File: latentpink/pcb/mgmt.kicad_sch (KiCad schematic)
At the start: 56 parts, among them J10 XILINX_JTAG, J11 FAN_01, J12 FAN_01, J15 CONN_01X03, J16 JUMPER_0402_SPDT, J17 JUMPER_0402_SPDT, J7 RJ45, U2 XC7K160T-2FBG484C, U20 AT24MAC402, U23 ADM3101E_QFN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

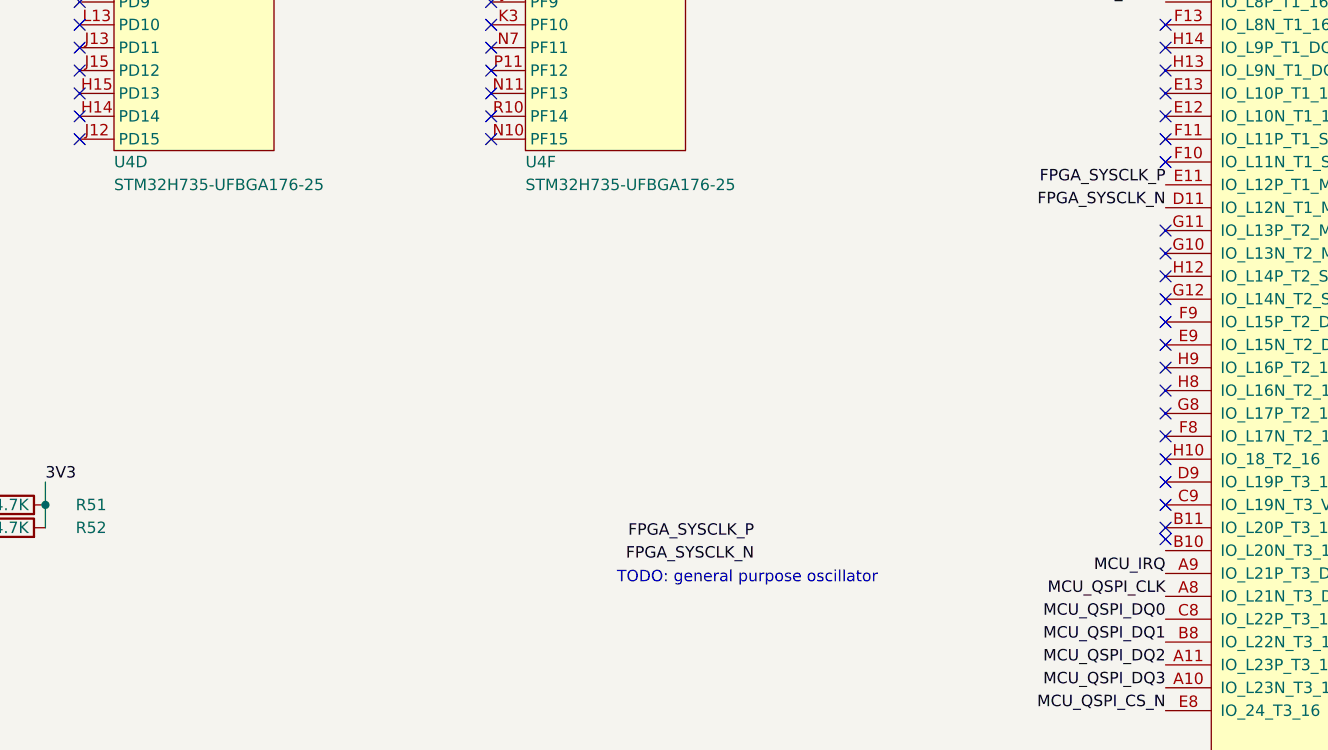
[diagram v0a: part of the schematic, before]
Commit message: Continued footprint assignment and miscellaneous missing tidbits of schematic
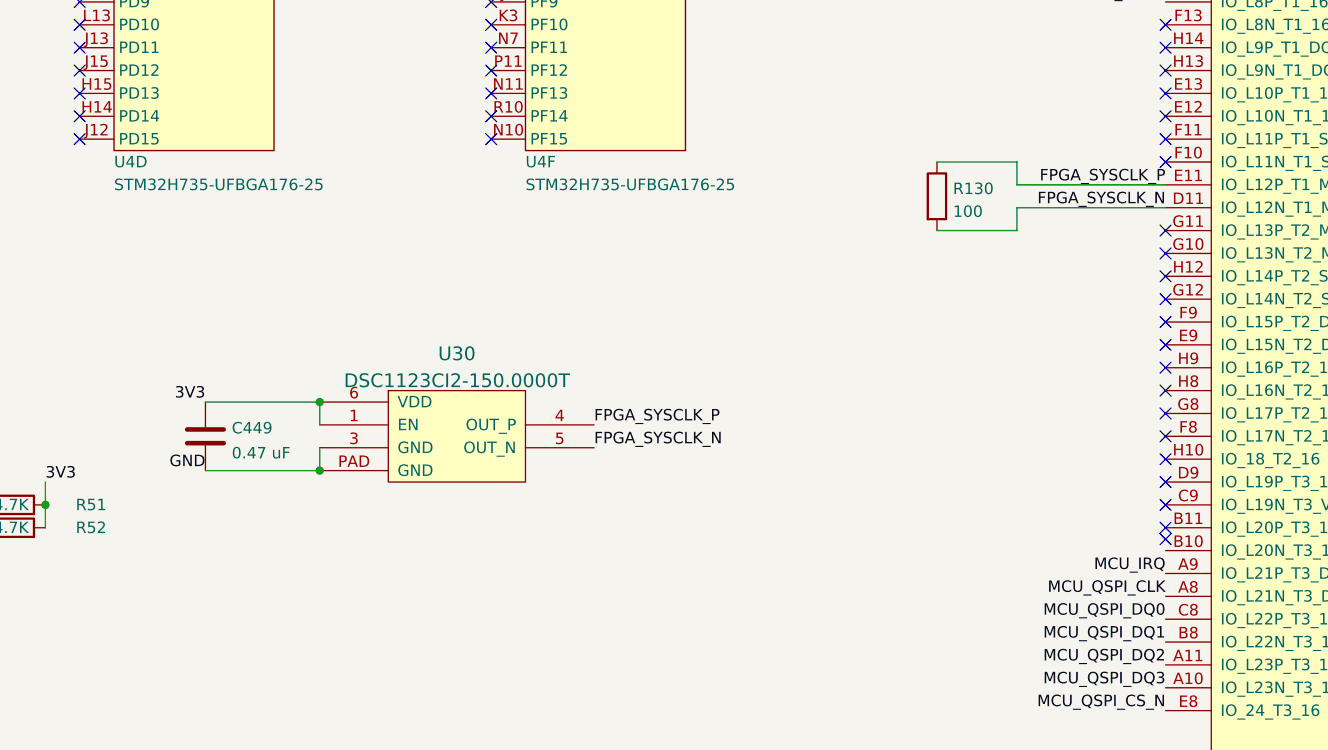
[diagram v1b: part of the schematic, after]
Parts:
- added C449: 0.47 uF, azonenberg_pcb:EIA_0402_CAP_NOSILK, symbol device:C
- added R130: 100, azonenberg_pcb:EIA_0402_RES_NOSILK, symbol device:R
- added U30: DSC1123CI2-150.0000T, azonenberg_pcb:OSCILLATOR_LVDS_3.2x2.5, symbol osc-azonenberg:OSC_LVDS
- C98, C99: footprint (none) -> azonenberg_pcb:EIA_1210_CAP_NOSILK
- J11, J12: footprint (none) -> azonenberg_pcb:CONN_MOLEX_KK_0470531000
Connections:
- net 3V3: now also C449.1, U30.1 (EN), U30.6 (VDD)
- net FPGA_SYSCLK_N: now also R130.2, U30.5 (OUT_N)
- net FPGA_SYSCLK_P: now also R130.1, U30.4 (OUT_P)
- net GND: now also C449.2, U30.3 (GND), U30.PAD (GND)
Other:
- note removed: "TODO: general purpose oscillator"
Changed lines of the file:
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@@
   (paper "A3")
   (title_block
-    (date "2023-05-16")
+    (date "2023-05-20")
     (rev "0.1")
     (company "Antikernel Labs")
@@
   (junction (at 31.75 66.04) (diameter 0) (color 0 0 0 0)
   )
+  (junction (at 241.3 158.75) (diameter 0) (color 0 0 0 0)
+  )
   (junction (at 139.7 55.88) (diameter 0) (color 0 0 0 0)
   )
@@
   (junction (at 76.2 90.17) (diameter 0) (color 0 0 0 0)
   )
+  (junction (at 241.3 151.13) (diameter 0) (color 0 0 0 0)
+  )
   (junction (at 62.23 38.1) (diameter 0) (color 0 0 0 0)
   )
@@
     (stroke (width 0) (type default) (color 0 0 0 0))
   )
+  (wire (pts (xy 318.77 132.08) (xy 309.88 132.08))
+    (stroke (width 0) (type default) (color 0 0 0 0))
+  )
   (wire (pts (xy 139.7 58.42) (xy 139.7 60.96))
     (stroke (width 0) (type default) (color 0 0 0 0))
@@
     (stroke (width 0) (type default) (color 0 0 0 0))
   )
+  (wire (pts (xy 241.3 158.75) (xy 241.3 156.21))
+    (stroke (width 0) (type default) (color 0 0 0 0))
+  )
   (wire (pts (xy 163.83 172.72) (xy 163.83 175.26))
     (stroke (width 0) (type default) (color 0 0 0 0))
@@
     (stroke (width 0) (type default) (color 0 0 0 0))
   )
+  (wire (pts (xy 335.28 127) (xy 318.77 127))
+    (stroke (width 0) (type default) (color 0 0 0 0))
+  )
   (wire (pts (xy 35.56 90.17) (xy 48.26 90.17))
     (stroke (width 0) (type default) (color 0 0 0 0))
@@
     (stroke (width 0) (type default) (color 0 0 0 0))
   )
+  (wire (pts (xy 335.28 129.54) (xy 318.77 129.54))
+    (stroke (width 0) (type default) (color 0 0 0 0))
+  )
   (wire (pts (xy 139.7 71.12) (xy 139.7 73.66))
     (stroke (width 0) (type default) (color 0 0 0 0))
   )
+  (wire (pts (xy 228.6 151.13) (xy 241.3 151.13))
+    (stroke (width 0) (type default) (color 0 0 0 0))
+  )
   (wire (pts (xy 35.56 181.61) (xy 46.99 181.61))
     (stroke (width 0) (type default) (color 0 0 0 0))
@@
     (stroke (width 0) (type default) (color 0 0 0 0))
   )
+  (wire (pts (xy 309.88 124.46) (xy 318.77 124.46))
+    (stroke (width 0) (type default) (color 0 0 0 0))
+  )
   (wire (pts (xy 139.7 68.58) (xy 139.7 71.12))
     (stroke (width 0) (type default) (color 0 0 0 0))
@@
     (stroke (width 0) (type default) (color 0 0 0 0))
   )
+  (wire (pts (xy 318.77 124.46) (xy 318.77 127))
+    (stroke (width 0) (type default) (color 0 0 0 0))
+  )
   (wire (pts (xy 114.3 48.26) (xy 114.3 50.8))
     (stroke (width 0) (type default) (color 0 0 0 0))
@@
     (stroke (width 0) (type default) (color 0 0 0 0))
   )
+  (wire (pts (xy 228.6 158.75) (xy 241.3 158.75))
+    (stroke (width 0) (type default) (color 0 0 0 0))
+  )
   (wire (pts (xy 139.7 45.72) (xy 139.7 48.26))
     (stroke (width 0) (type default) (color 0 0 0 0))
@@
     (stroke (width 0) (type default) (color 0 0 0 0))
   )
+  (wire (pts (xy 241.3 151.13) (xy 241.3 153.67))
+    (stroke (width 0) (type default) (color 0 0 0 0))
+  )
   (wire (pts (xy 100.33 148.59) (xy 100.33 151.13))
     (stroke (width 0) (type default) (color 0 0 0 0))
@@
     (stroke (width 0) (type default) (color 0 0 0 0))
   )
+  (wire (pts (xy 318.77 129.54) (xy 318.77 132.08))
+    (stroke (width 0) (type default) (color 0 0 0 0))
+  )
   (wire (pts (xy 62.23 97.79) (xy 76.2 97.79))
     (stroke (width 0) (type default) (color 0 0 0 0))
@@
     (effects (font (size 1.27 1.27)) (justify left bottom))
   )
-  (text "TODO: general purpose oscillator" (at 274.32 171.45 0)
-    (effects (font (size 1.27 1.27)) (justify left bottom))
-  )
   (text "MCU VDDA decoupling" (at 35.56 120.65 0)
     (effects (font (size 1.27 1.27)) (justify left bottom))
@@
     (effects (font (size 1.27 1.27)) (justify left bottom))
   )
-  (label "FPGA_SYSCLK_N" (at 289.56 168.91 180)
-    (effects (font (size 1.27 1.27)) (justify right bottom))
+  (label "FPGA_SYSCLK_N" (at 271.78 156.21 0)
+    (effects (font (size 1.27 1.27)) (justify left bottom))
   )
   (label "GND" (at 162.56 170.18 180)
@@
     (effects (font (size 1.27 1.27)) (justify left bottom))
   )
+  (label "3V3" (at 228.6 151.13 180)
+    (effects (font (size 1.27 1.27)) (justify right bottom))
+  )
   (label "RS232_TX" (at 208.28 228.6 180)
     (effects (font (size 1.27 1.27)) (justify right bottom))
@@
     (effects (font (size 1.27 1.27)) (justify right bottom))
   )
-  (label "FPGA_SYSCLK_P" (at 289.56 166.37 180)
-    (effects (font (size 1.27 1.27)) (justify right bottom))
+  (label "FPGA_SYSCLK_P" (at 271.78 153.67 0)
+    (effects (font (size 1.27 1.27)) (justify left bottom))
   )
   (label "RS232_TX" (at 157.48 212.09 0)
@@
     (effects (font (size 1.27 1.27)) (justify right bottom))
   )
+  (label "GND" (at 228.6 158.75 180)
+    (effects (font (size 1.27 1.27)) (justify right bottom))
+  )
   (label "3V3" (at 163.83 162.56 180)
     (effects (font (size 1.27 1.27)) (justify right bottom))
@@
       (effects (font (size 1.27 1.27)) (justify left))
     )
-    (property "Footprint" "" (id 2) (at 77.1652 264.16 0)
+    (property "Footprint" "azonenberg_pcb:EIA_1210_CAP_NOSILK" (id 2) (at 77.1652 264.16 0)
       (effects (font (size 1.27 1.27)) hide)
     )
@@
       (effects (font (size 1.27 1.27)) (justify left))
     )
-    (property "Footprint" "" (id 2) (at 94.9452 264.16 0)
+    (property "Footprint" "azonenberg_pcb:EIA_1210_CAP_NOSILK" (id 2) (at 94.9452 264.16 0)
       (effects (font (size 1.27 1.27)) hide)
     )
@@
       (effects (font (size 1.27 1.27)) (justify left))
     )
-    (property "Footprint" "" (id 2) (at 60.96 259.08 0)
+    (property "Footprint" "azonenberg_pcb:CONN_MOLEX_KK_0470531000" (id 2) (at 60.96 259.08 0)
       (effects (font (size 1.27 1.27)) hide)
     )
@@
     (pin "2")
   )
+  (symbol (lib_id "device:C") (at 228.6 154.94 0) (unit 1)
+    (in_bom yes) (on_board yes) (fields_autoplaced)
+    (property "Reference" "C449" (id 0) (at 231.521 154.0315 0)
+      (effects (font (size 1.27 1.27)) (justify left))
+    )
+    (property "Value" "0.47 uF" (id 1) (at 231.521 156.8066 0)
+      (effects (font (size 1.27 1.27)) (justify left))
+    )
+    (property "Footprint" "azonenberg_pcb:EIA_0402_CAP_NOSILK" (id 2) (at 229.5652 158.75 0)
+      (effects (font (size 1.27 1.27)) hide)
+    )
+    (property "Datasheet" "" (id 3) (at 228.6 154.94 0)
+      (effects (font (size 1.27 1.27)) hide)
+    )
+    (pin "1")
+    (pin "2")
+  )
   (symbol (lib_id "device:C") (at 46.99 207.01 0) (unit 1)
     (in_bom yes) (on_board yes) (fields_autoplaced)
@@
       (effects (font (size 1.27 1.27)) (justify left))
     )
-    (property "Footprint" "" (id 2) (at 33.02 259.08 0)
+    (property "Footprint" "azonenberg_pcb:CONN_MOLEX_KK_0470531000" (id 2) (at 33.02 259.08 0)
       (effects (font (size 1.27 1.27)) hide)
     )
@@
     (pin "2")
   )
+  (symbol (lib_id "device:R") (at 309.88 128.27 0) (unit 1)
+    (in_bom yes) (on_board yes) (fields_autoplaced)
+    (property "Reference" "R130" (id 0) (at 311.658 127.4353 0)
+      (effects (font (size 1.27 1.27)) (justify left))
+    )
+    (property "Value" "100" (id 1) (at 311.658 129.9722 0)
+      (effects (font (size 1.27 1.27)) (justify left))
+    )
+    (property "Footprint" "azonenberg_pcb:EIA_0402_RES_NOSILK" (id 2) (at 308.102 128.27 90)
+      (effects (font (size 1.27 1.27)) hide)
+    )
+    (property "Datasheet" "" (id 3) (at 309.88 128.27 0)
+      (effects (font (size 1.27 1.27)) hide)
+    )
+    (pin "1")
+    (pin "2")
+  )
   (symbol (lib_id "device:C") (at 62.23 101.6 0) (unit 1)
     (in_bom yes) (on_board yes) (fields_autoplaced)
@@
     (pin "M3")
   )
+  (symbol (lib_id "osc-azonenberg:OSC_LVDS") (at 248.92 160.02 0) (unit 1)
+    (in_bom yes) (on_board yes) (fields_autoplaced)
+    (property "Reference" "U30" (id 0) (at 256.54 145.7759 0)
+      (effects (font (size 1.524 1.524)))
+    )
+    (property "Value" "DSC1123CI2-150.0000T" (id 1) (at 256.54 148.7693 0)
+      (effects (font (size 1.524 1.524)))
+    )
+    (property "Footprint" "azonenberg_pcb:OSCILLATOR_LVDS_3.2x2.5" (id 2) (at 248.92 160.02 0)
+      (effects (font (size 1.524 1.524)) hide)
+    )
+    (property "Datasheet" "" (id 3) (at 248.92 160.02 0)
+      (effects (font (size 1.524 1.524)))
+    )
+    (pin "1")
+    (pin "3")
+    (pin "4")
+    (pin "5")
+    (pin "6")
+    (pin "PAD")
+  )
   (symbol (lib_id "device:C") (at 74.93 128.27 0) (unit 1)
